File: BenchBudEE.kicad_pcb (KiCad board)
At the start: 4 copper layers, 165.1 x 63.5 mm, 115 parts, among them K1 1461069-5, P1 24-pin Mini-Fit Jr., P2 CONN_2, P3 CONN_3X2, P4 12-pin Terminal Block, P5 3-pin TB, Q1 2N3404, Q2 DMN65D8L-7, Q3 AOD476, Q4 AOD476, SW1 Power Switch, U1 LTV-816S, U10 LMT84, U11 OPA4170, U3 LM317T, U4 LM317T, U5 LM337T, U6 LM337T, U8 MCP4801, U9 MCP3901

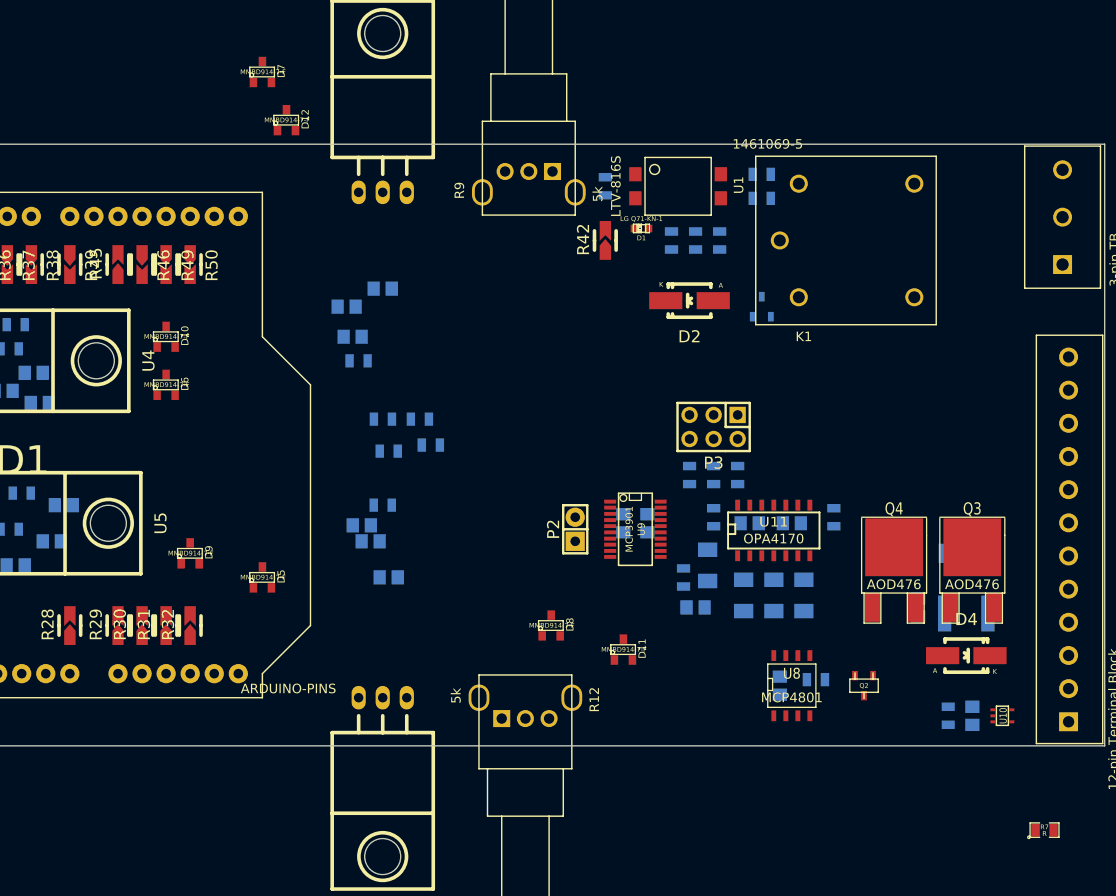
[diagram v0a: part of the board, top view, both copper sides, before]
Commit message: Associated and placed the LED Driver Module
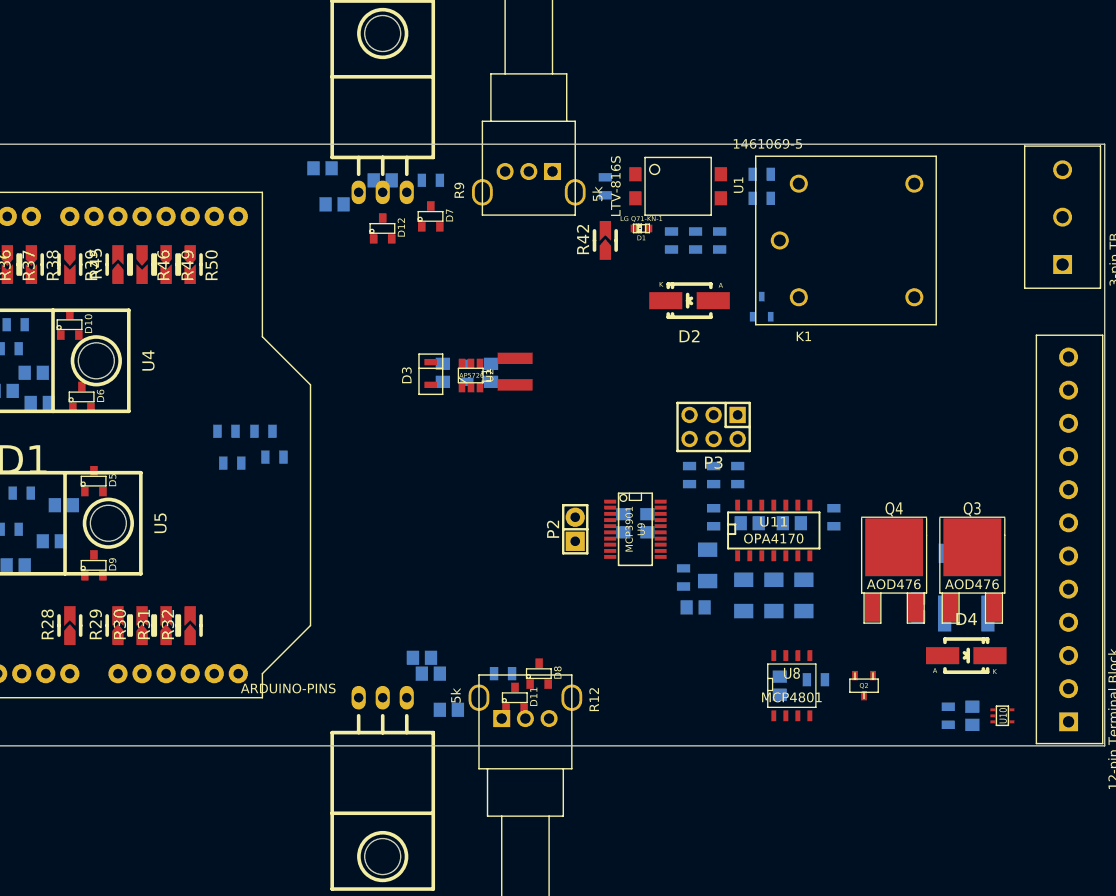
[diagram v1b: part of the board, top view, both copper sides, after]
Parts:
- added C1: 1u, Capacitors_SMD:c_0805, B.Cu at (229.9, 135.9)
- added C2: 1u, Capacitors_SMD:c_0805, B.Cu at (224.8, 135.9)
- added D3: BO540WS-7, BenchBudEE:SOD-323, F.Cu at (223.5, 137.2)
- added L1: 22u, BenchBudEE:NR4012, F.Cu at (232.4, 137.2)
- added U2: AP5726, SMD_Packages:SOT23_6, F.Cu at (227.8, 136.2)
- R7: value R -> 15; moved to B.Cu
- moved R7 77.8 mm to (227.3, 135.9), turned to 270 degrees
- moved D7 23.4 mm to (223.5, 119.4)
- moved R11 21.8 mm to (231.1, 167.6)
- moved R10 20.5 mm to (223.5, 115.6)
- moved D5 20.5 mm to (188.0, 147.3)
- moved C15 16.8 mm to (218.4, 115.6)
- moved R15 16.6 mm to (202.0, 142.1)
- moved R17 16.6 mm to (205.9, 142.1)
- moved R18 16.6 mm to (207.0, 144.8)
- moved R16 16.6 mm to (202.6, 145.4)
- moved C17 15.3 mm to (225.4, 171.4)
- moved C21 15.3 mm to (223.5, 167.6)
- moved C25 15.3 mm to (222.6, 166.0)
- moved D12 15.3 mm to (218.4, 120.7)
- moved C24 14.2 mm to (212.1, 114.3)
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
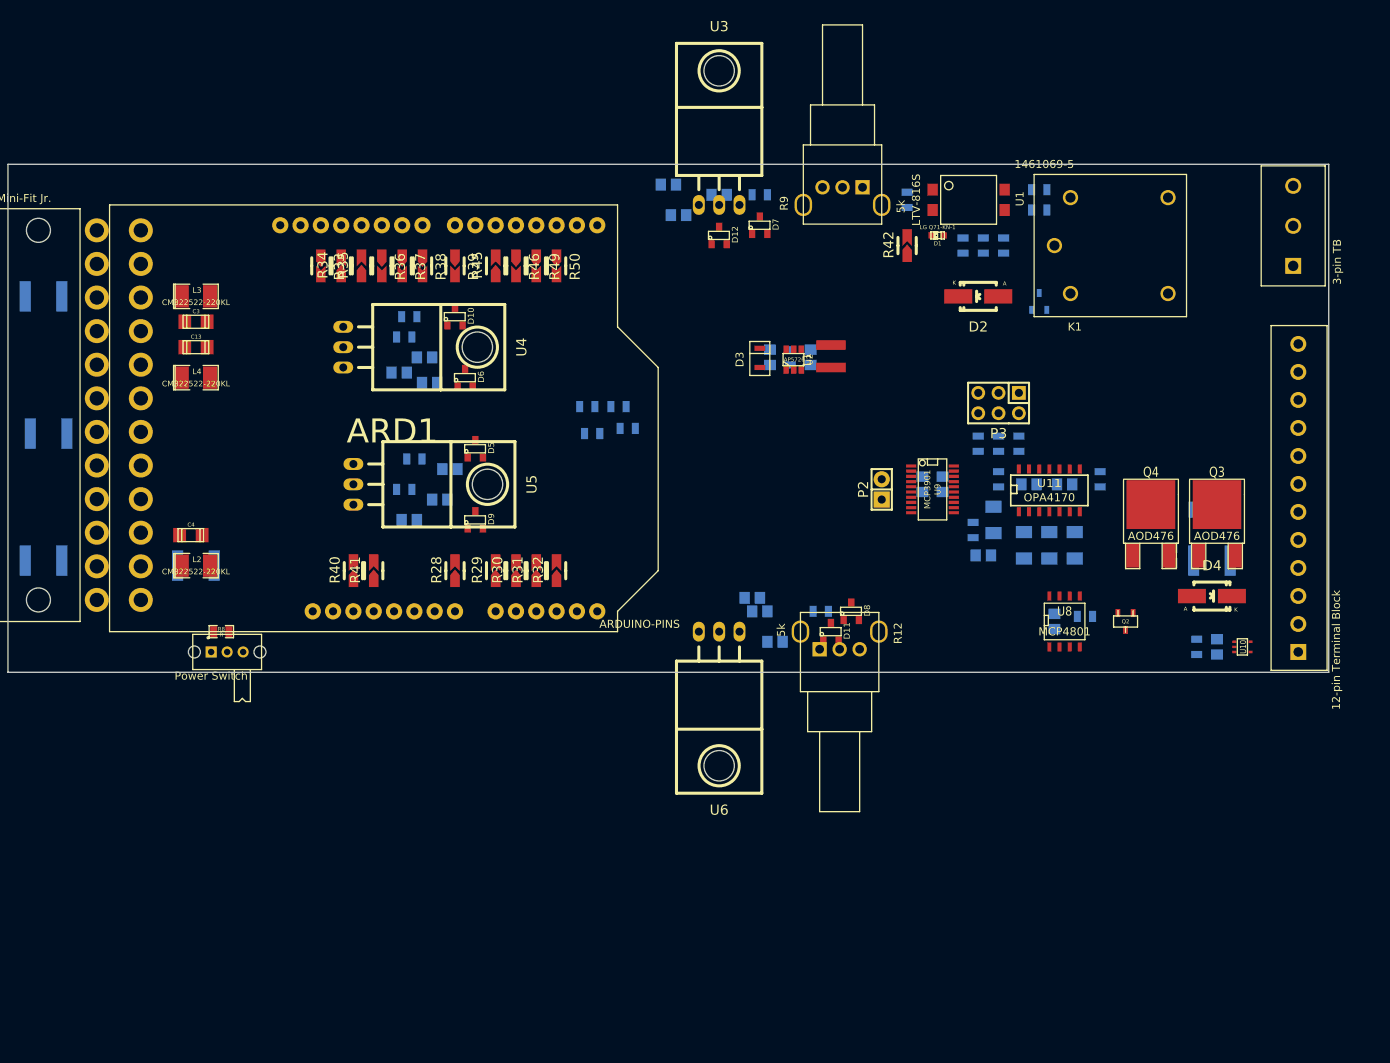
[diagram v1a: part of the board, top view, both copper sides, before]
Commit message: Rearranged layout a bit and added heatsinks
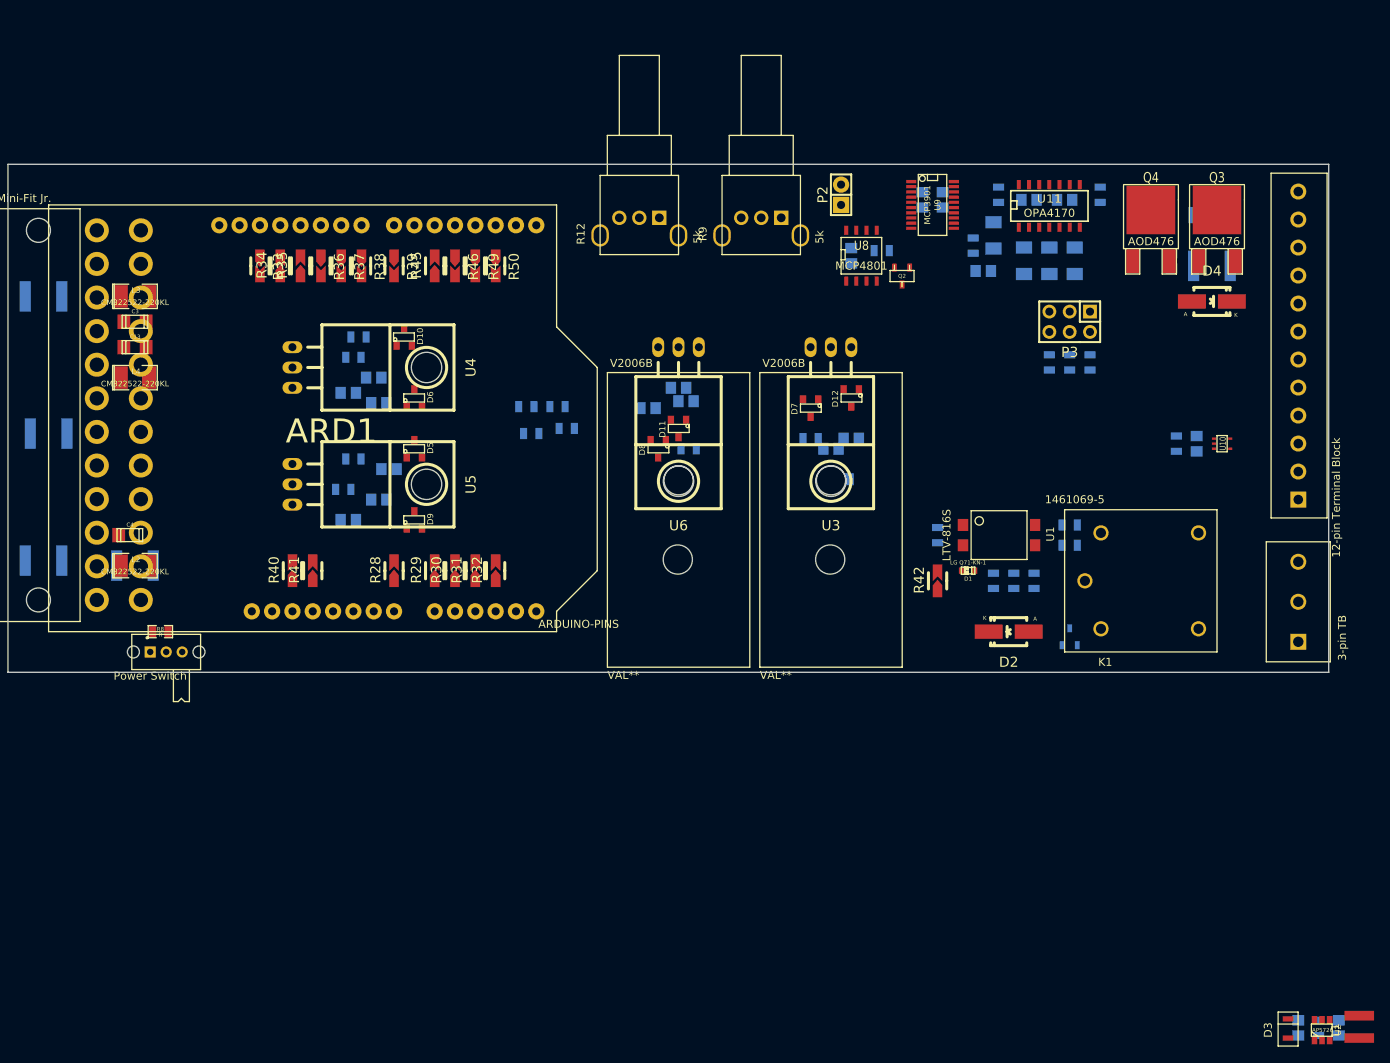
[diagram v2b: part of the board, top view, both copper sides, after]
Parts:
- added V2006B: VAL**, BenchBudEE:V2006B, F.Cu at (204.5, 174.6)
- added V2006B: VAL**, BenchBudEE:V2006B, F.Cu at (223.5, 174.6)
- moved C1 106.7 mm to (295.9, 219.7)
- moved C2 106.7 mm to (290.8, 219.7)
- moved R7 106.7 mm to (293.4, 219.7)
- moved U2 106.7 mm to (293.8, 220.0)
- moved D3 106.7 mm to (289.6, 221.0)
- moved L1 106.7 mm to (298.4, 221.0)
- moved C11 52.3 mm to (234.9, 123.2)
- moved R19 52.3 mm to (238.8, 122.6)
- moved U8 52.3 mm to (236.2, 123.2)
- moved R12 51.8 mm to (213.4, 120.7), turned to 90 degrees
- moved Q2 51.4 mm to (241.3, 125.7)
- moved P5 47.0 mm to (290.8, 171.4)
- moved C24 42.7 mm to (233.7, 151.1), turned to 180 degrees
- moved K1 42.1 mm to (264.2, 163.8)
- moved R1 42.1 mm to (245.7, 158.1)
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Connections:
- P4 pad 10: /TerminalBlock/TACH_IN -> /Fan/TACH_IN

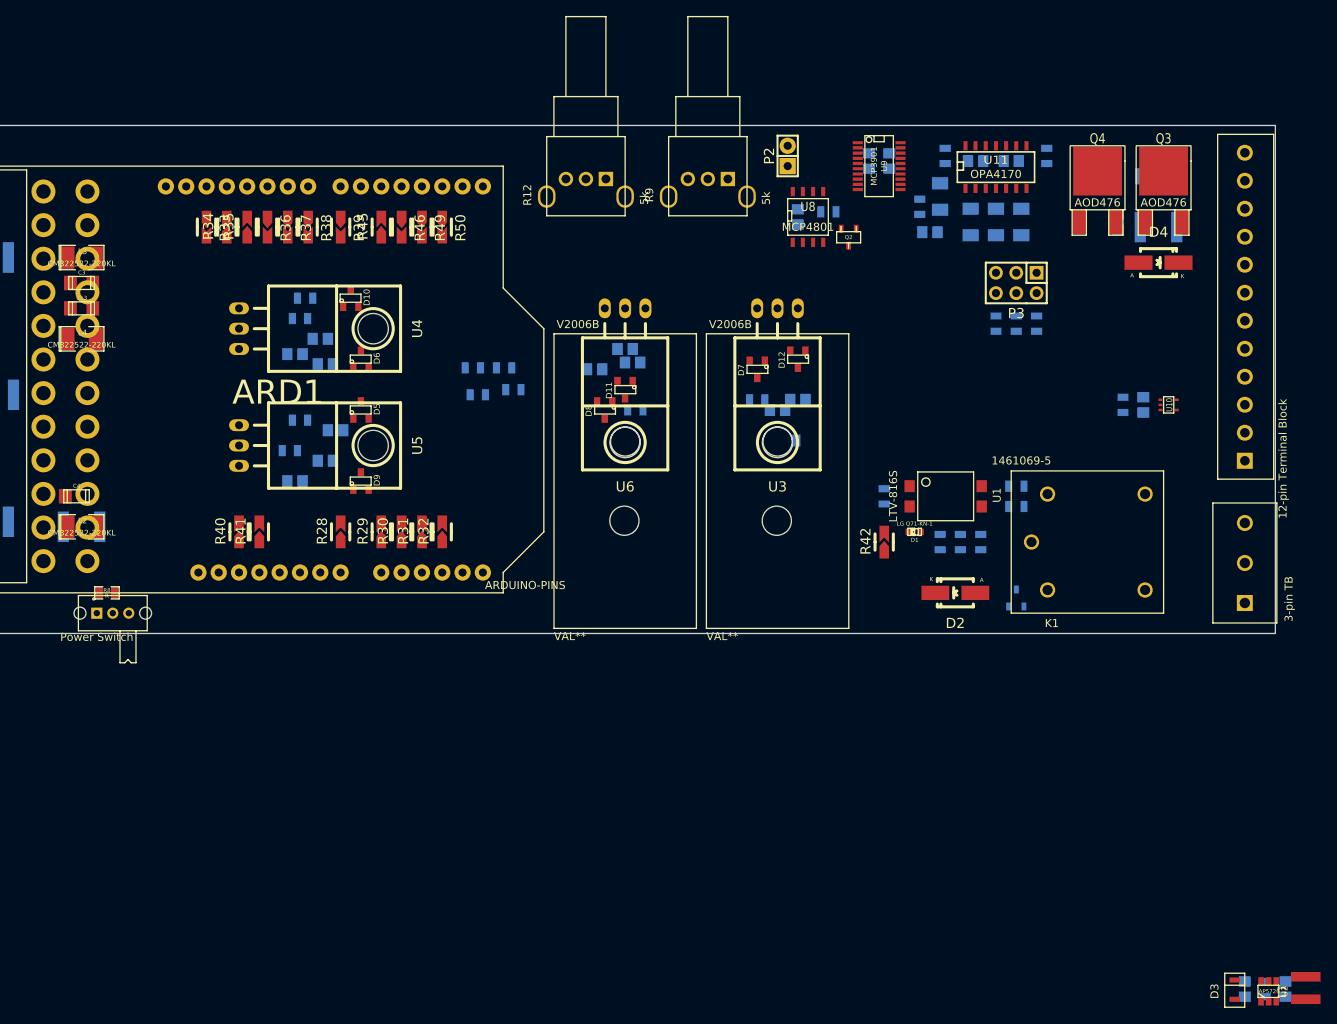
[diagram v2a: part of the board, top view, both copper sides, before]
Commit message: Various minor updates after Ground and Power Planes video
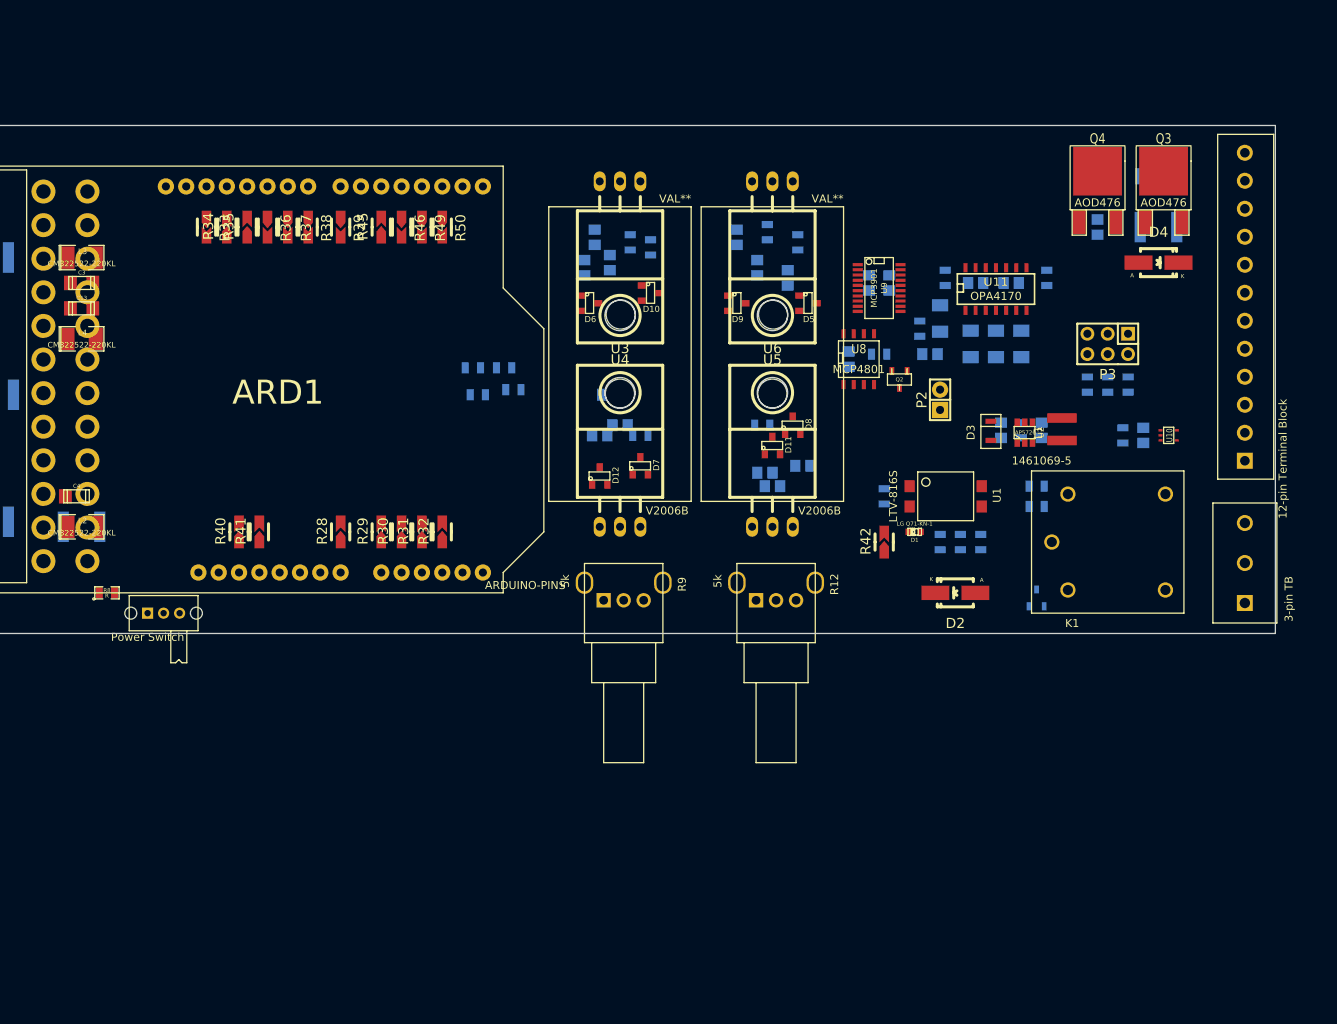
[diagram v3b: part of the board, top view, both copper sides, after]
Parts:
- moved U2 76.2 mm to (263.3, 150.1)
- moved C1 76.2 mm to (265.4, 149.9)
- moved D3 76.2 mm to (259.1, 151.1)
- moved R7 76.2 mm to (262.9, 149.9)
- moved C2 76.2 mm to (260.4, 149.9)
- moved L1 76.2 mm to (268.0, 151.1)
- moved U5 74.4 mm to (231.8, 118.7), turned to 180 degrees
- moved R53 66.1 mm to (234.9, 126.4), turned to 270 degrees
- moved R54 65.6 mm to (231.1, 125.1), turned to 270 degrees
- moved V2006B 63.9 mm to (240.7, 121.9), turned to 180 degrees
- moved C18 63.1 mm to (227.3, 125.7), turned to 270 degrees
- moved C14 59.6 mm to (233.7, 130.8), turned to 270 degrees
- moved C22 59.1 mm to (229.9, 129.5), turned to 270 degrees
- moved D5 57.4 mm to (236.2, 134.0), turned to 270 degrees
- moved V2006B 52.7 mm to (221.6, 121.9), turned to 180 degrees
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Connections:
- C1 pad 1: +5V -> +5P
- C12 pad 1: AGND -> GND
- C8 pad 2: -12V -> FE_V-
- C9 pad 2: +12V -> FE_V+
- L1 pad 1: +5V -> +5P
- P4 pad 1: +3.3V -> /LED_Driver/LED_STRING+
- P4 pad 11: /TerminalBlock/TC_IN+ -> /Fan/FAN_OUT-
- P4 pad 12: /TerminalBlock/TC_IN- -> /Fan/FAN_OUT+
- P4 pad 2: +5V -> /LED_Driver/LED_STRING-
- P4 pad 6: /LED_Driver/LED_STRING+ -> +3.3V
- P4 pad 7: /LED_Driver/LED_STRING- -> +5V
- P4 pad 8: /Fan/FAN_OUT+ -> /TerminalBlock/TC_IN+
- P4 pad 9: /Fan/FAN_OUT- -> /TerminalBlock/TC_IN-
- Q3 pad 3: AGND -> GND
- R20 pad 2: AGND -> GND
- U11 pad 11: -12V -> FE_V-
- U11 pad 4: +12V -> FE_V+
- U2 pad 6: +5V -> +5P

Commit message: Updates from Reality Check video
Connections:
- K1 pad 3: /Relay/RELAY_NO -> /Relay/RELAY_NC
- K1 pad 4: /TerminalBlock/RELAY_COM -> /Relay/RELAY_NO
- P5 pad 2: /TerminalBlock/RELAY_COM -> /Relay/RELAY_COM
- P5 pad 3: /Relay/RELAY_COM -> /Relay/RELAY_NC
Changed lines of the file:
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@@
   (net 32 /PowerAdjustmentMonitor/V-_ADJ)
   (net 33 /Relay/RELAY_COM)
-  (net 34 /Relay/RELAY_NO)
-  (net 35 /TerminalBlock/RELAY_COM)
+  (net 34 /Relay/RELAY_NC)
+  (net 35 /Relay/RELAY_NO)
   (net 36 /TerminalBlock/TC_IN+)
   (net 37 /TerminalBlock/TC_IN-)
@@
     (add_net /PowerAdjustmentMonitor/V-_ADJ)
     (add_net /Relay/RELAY_COM)
+    (add_net /Relay/RELAY_NC)
     (add_net /Relay/RELAY_NO)
-    (add_net /TerminalBlock/RELAY_COM)
     (add_net /TerminalBlock/TC_IN+)
     (add_net /TerminalBlock/TC_IN-)
@@
       (net 82 "Net-(D2-Pad2)"))
     (pad 3 thru_hole circle (at 14.1986 -5.9944) (size 1.905 1.905) (drill 1.27) (layers *.Cu *.Mask F.SilkS)
-      (net 34 /Relay/RELAY_NO))
+      (net 34 /Relay/RELAY_NC))
     (pad 4 thru_hole circle (at 14.1986 5.9944) (size 1.905 1.905) (drill 1.27) (layers *.Cu *.Mask F.SilkS)
-      (net 35 /TerminalBlock/RELAY_COM))
+      (net 35 /Relay/RELAY_NO))
     (pad 5 thru_hole circle (at 2.0066 5.9944) (size 1.905 1.905) (drill 1.27) (layers *.Cu *.Mask F.SilkS)
       (net 81 "Net-(D2-Pad1)"))
@@
     (fp_line (start 12.5 -4) (end 12.5 4) (layer F.SilkS) (width 0.15))
     (pad 1 thru_hole rect (at 0 0 90) (size 2 2) (drill 1.3) (layers *.Cu *.Mask F.SilkS)
-      (net 34 /Relay/RELAY_NO))
+      (net 35 /Relay/RELAY_NO))
     (pad 2 thru_hole circle (at 5 0 90) (size 2 2) (drill 1.3) (layers *.Cu *.Mask F.SilkS)
-      (net 35 /TerminalBlock/RELAY_COM))
+      (net 33 /Relay/RELAY_COM))
     (pad 3 thru_hole circle (at 10 0 90) (size 2 2) (drill 1.3) (layers *.Cu *.Mask F.SilkS)
-      (net 33 /Relay/RELAY_COM))
+      (net 34 /Relay/RELAY_NC))
   )
   (module BenchBudEE:ATX_Header (layer F.Cu)

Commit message: Updates from Layout Work Session 2 video and KiCAD update
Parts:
- removed V2006B (x2): VAL**, BenchBudEE:V2006B
- added 3 mm: VAL**, BenchBudEE:3mm-NPTH, F.Cu at (223.5, 54.6)
- added 3 mm: VAL**, BenchBudEE:3mm-NPTH, F.Cu at (85.1, 110.5)
- added 3 mm: VAL**, BenchBudEE:3mm-NPTH, F.Cu at (85.1, 54.6)
- U3, U4, U5, U6: footprint Transistors_TO-220:TO-220_Neutral123_Horizontal -> Transistors_TO-220:TO-220_Neutral123_Vertical
- moved C1 165.2 mm to (301.0, -11.4)
- moved C2 165.2 mm to (295.9, -11.4)
- moved C7 165.2 mm to (287.0, -21.0)
- moved P2 165.2 mm to (288.3, -15.2)
- moved R19 165.2 mm to (280.7, -21.0)
- moved R26 165.2 mm to (306.7, -17.1)
- moved R43 165.2 mm to (309.2, -17.1)
- moved R44 165.2 mm to (311.8, -17.1)
- moved R7 165.2 mm to (298.4, -11.4)
- moved U11 165.2 mm to (295.3, -29.2)
- moved U9 165.2 mm to (280.7, -29.2)
- moved C10 165.2 mm to (313.7, -10.8)
- moved C11 165.2 mm to (276.9, -20.3)
- moved C5 165.2 mm to (281.9, -29.8)
- moved C6 165.2 mm to (279.4, -29.8)
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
